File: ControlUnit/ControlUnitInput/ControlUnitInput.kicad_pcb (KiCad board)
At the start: 2 copper layers, 100.1 x 90 mm, 41 parts, among them J1 Conn_02x15_Odd_Even, J2 Conn_01x02, SW1 SW_Push, SW10 SW_Push, SW11 SW_Push, SW12 SW_Push, SW13 SW_Push, SW14 SW_Push, SW15 SW_Push, SW16 SW_Push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

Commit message: add schematic for LEDs controller
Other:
- board text added: "Board design by Keroth & CodingSpiderFox License: CERN OHL v1.2"
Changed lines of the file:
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@@
     (area 10.289181 12.624999 112.851001 102.775001)
     (thickness 1.6)
-    (drawings 4)
+    (drawings 5)
     (tracks 240)
     (zones 0)
@@
     )
   )
+  (gr_text "Board design by Keroth & CodingSpiderFox\nLicense: CERN OHL v1.2" (at 109.601 46.863 90) (layer F.Fab)
+    (effects (font (size 1.016 1.016) (thickness 0.254)))
+  )
   (gr_line (start 112.776 12.7) (end 112.776 102.7) (angle 90) (layer Edge.Cuts) (width 0.15))

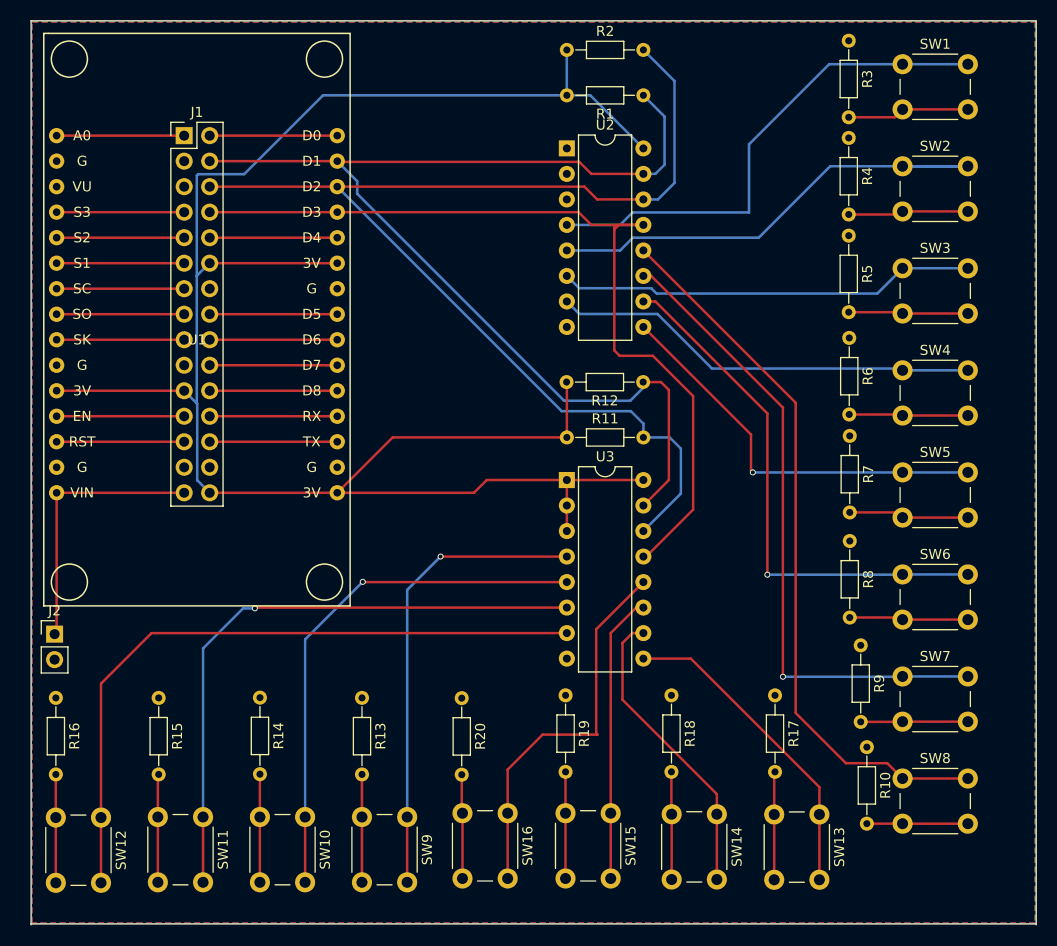
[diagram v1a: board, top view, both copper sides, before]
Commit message: clarify power connector voltages add license information and revisions to boards
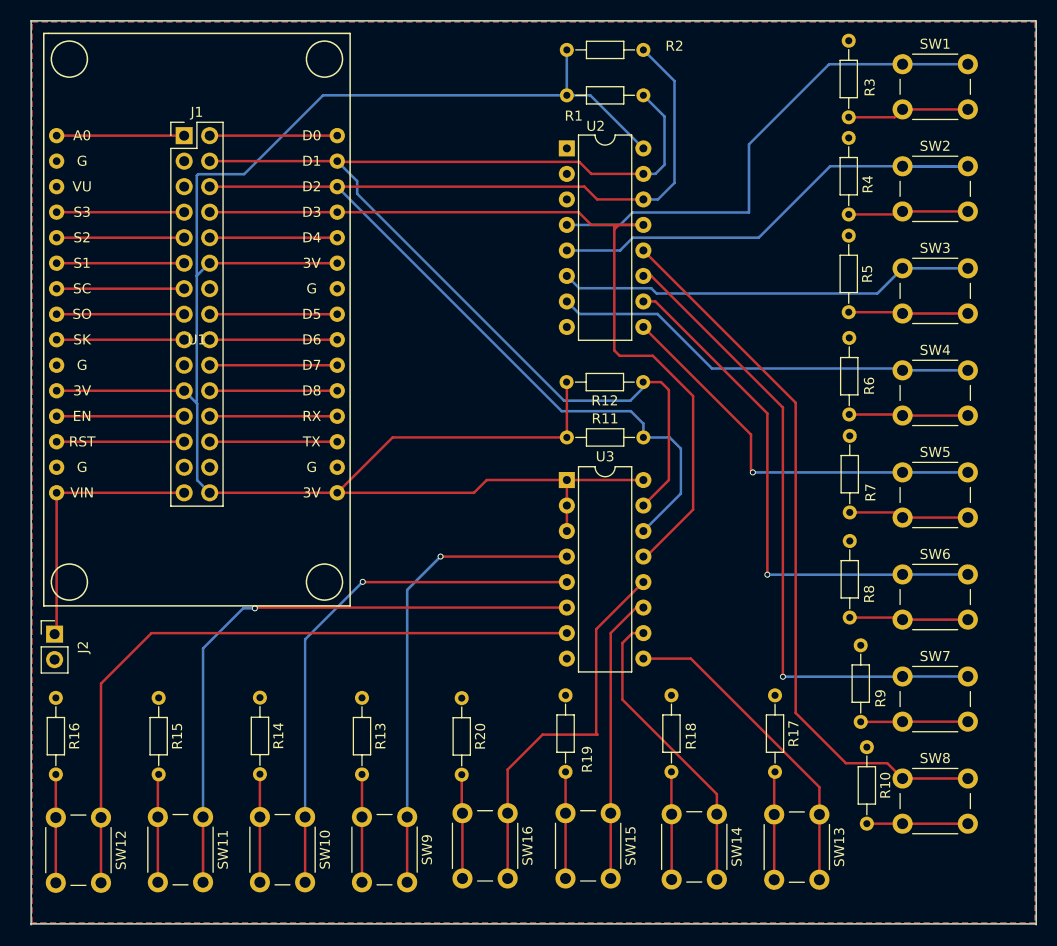
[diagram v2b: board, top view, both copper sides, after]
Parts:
- J1: value Conn_02x15_Odd_Even -> (none)
- J2: value Conn_01x02 -> (none)
- SW12: value SW_Push -> (none)
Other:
- board text added: "5V"
- board text added: "Rev 0.1"
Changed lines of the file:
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@@
     (links 139)
     (no_connects 0)
-    (area 10.289181 12.624999 112.851001 102.775001)
+    (area 11.9846 12.624999 112.851001 102.775001)
     (thickness 1.6)
-    (drawings 5)
+    (drawings 7)
     (tracks 240)
     (zones 0)
@@
       (effects (font (size 1 1) (thickness 0.15)))
     )
-    (fp_text value Conn_02x15_Odd_Even (at 1.27 37.89) (layer F.Fab)
+    (fp_text value "" (at 1.27 37.89) (layer F.Fab)
       (effects (font (size 1 1) (thickness 0.15)))
     )
@@
     (descr "Through hole straight pin header, 1x02, 2.54mm pitch, single row")
     (tags "Through hole pin header THT 1x02 2.54mm single row")
-    (fp_text reference J2 (at 0 -2.33) (layer F.SilkS)
-      (effects (font (size 1 1) (thickness 0.15)))
-    )
-    (fp_text value Conn_01x02 (at 0 4.87) (layer F.Fab)
+    (fp_text reference J2 (at 2.8448 1.2954 90) (layer F.SilkS)
+      (effects (font (size 1 1) (thickness 0.15)))
+    )
+    (fp_text value "" (at 0 4.87) (layer F.Fab)
       (effects (font (size 1 1) (thickness 0.15)))
     )
@@
     (descr "Resistor, Axial_DIN0204 series, Axial, Horizontal, pin pitch=7.62mm, 0.16666666666666666W = 1/6W, length*diameter=3.6*1.6mm^2, http://cdn-reichelt.de/documents/datenblatt/B400/1_4W%23YAG.pdf")
     (tags "Resistor Axial_DIN0204 series Axial Horizontal pin pitch 7.62mm 0.16666666666666666W = 1/6W length 3.6mm diameter 1.6mm")
-    (fp_text reference R1 (at 3.81 -1.86 180) (layer F.SilkS)
+    (fp_text reference R1 (at 6.9342 -2.0574 180) (layer F.SilkS)
       (effects (font (size 1 1) (thickness 0.15)))
     )
@@
     (descr "Resistor, Axial_DIN0204 series, Axial, Horizontal, pin pitch=7.62mm, 0.16666666666666666W = 1/6W, length*diameter=3.6*1.6mm^2, http://cdn-reichelt.de/documents/datenblatt/B400/1_4W%23YAG.pdf")
     (tags "Resistor Axial_DIN0204 series Axial Horizontal pin pitch 7.62mm 0.16666666666666666W = 1/6W length 3.6mm diameter 1.6mm")
-    (fp_text reference R2 (at 3.81 -1.86) (layer F.SilkS)
-      (effects (font (size 1 1) (thickness 0.15)))
-    )
-    (fp_text value 4.7k (at 3.81 1.86) (layer F.Fab)
+    (fp_text reference R2 (at 10.7188 -0.381) (layer F.SilkS)
+      (effects (font (size 1 1) (thickness 0.15)))
+    )
+    (fp_text value 4.7k (at -3.7846 -0.0254) (layer F.Fab)
       (effects (font (size 1 1) (thickness 0.15)))
     )
@@
     (descr "Resistor, Axial_DIN0204 series, Axial, Horizontal, pin pitch=7.62mm, 0.16666666666666666W = 1/6W, length*diameter=3.6*1.6mm^2, http://cdn-reichelt.de/documents/datenblatt/B400/1_4W%23YAG.pdf")
     (tags "Resistor Axial_DIN0204 series Axial Horizontal pin pitch 7.62mm 0.16666666666666666W = 1/6W length 3.6mm diameter 1.6mm")
-    (fp_text reference R3 (at 3.81 -1.86 270) (layer F.SilkS)
+    (fp_text reference R3 (at 4.6482 -2.1082 270) (layer F.SilkS)
       (effects (font (size 1 1) (thickness 0.15)))
     )
@@
     (descr "Resistor, Axial_DIN0204 series, Axial, Horizontal, pin pitch=7.62mm, 0.16666666666666666W = 1/6W, length*diameter=3.6*1.6mm^2, http://cdn-reichelt.de/documents/datenblatt/B400/1_4W%23YAG.pdf")
     (tags "Resistor Axial_DIN0204 series Axial Horizontal pin pitch 7.62mm 0.16666666666666666W = 1/6W length 3.6mm diameter 1.6mm")
-    (fp_text reference R4 (at 3.81 -1.86 270) (layer F.SilkS)
+    (fp_text reference R4 (at 4.6228 -1.905 270) (layer F.SilkS)
       (effects (font (size 1 1) (thickness 0.15)))
     )
@@
     (descr "Resistor, Axial_DIN0204 series, Axial, Horizontal, pin pitch=7.62mm, 0.16666666666666666W = 1/6W, length*diameter=3.6*1.6mm^2, http://cdn-reichelt.de/documents/datenblatt/B400/1_4W%23YAG.pdf")
     (tags "Resistor Axial_DIN0204 series Axial Horizontal pin pitch 7.62mm 0.16666666666666666W = 1/6W length 3.6mm diameter 1.6mm")
-    (fp_text reference R6 (at 3.81 -1.86 270) (layer F.SilkS)
+    (fp_text reference R6 (at 4.7752 -2.0066 270) (layer F.SilkS)
       (effects (font (size 1 1) (thickness 0.15)))
     )
@@
     (descr "Resistor, Axial_DIN0204 series, Axial, Horizontal, pin pitch=7.62mm, 0.16666666666666666W = 1/6W, length*diameter=3.6*1.6mm^2, http://cdn-reichelt.de/documents/datenblatt/B400/1_4W%23YAG.pdf")
     (tags "Resistor Axial_DIN0204 series Axial Horizontal pin pitch 7.62mm 0.16666666666666666W = 1/6W length 3.6mm diameter 1.6mm")
-    (fp_text reference R7 (at 3.81 -1.86 270) (layer F.SilkS)
+    (fp_text reference R7 (at 5.6388 -2.0828 270) (layer F.SilkS)
       (effects (font (size 1 1) (thickness 0.15)))
     )
@@
     (descr "Resistor, Axial_DIN0204 series, Axial, Horizontal, pin pitch=7.62mm, 0.16666666666666666W = 1/6W, length*diameter=3.6*1.6mm^2, http://cdn-reichelt.de/documents/datenblatt/B400/1_4W%23YAG.pdf")
     (tags "Resistor Axial_DIN0204 series Axial Horizontal pin pitch 7.62mm 0.16666666666666666W = 1/6W length 3.6mm diameter 1.6mm")
-    (fp_text reference R8 (at 3.81 -1.86 270) (layer F.SilkS)
+    (fp_text reference R8 (at 5.2832 -1.9558 270) (layer F.SilkS)
       (effects (font (size 1 1) (thickness 0.15)))
     )
@@
     (descr "Resistor, Axial_DIN0204 series, Axial, Horizontal, pin pitch=7.62mm, 0.16666666666666666W = 1/6W, length*diameter=3.6*1.6mm^2, http://cdn-reichelt.de/documents/datenblatt/B400/1_4W%23YAG.pdf")
     (tags "Resistor Axial_DIN0204 series Axial Horizontal pin pitch 7.62mm 0.16666666666666666W = 1/6W length 3.6mm diameter 1.6mm")
-    (fp_text reference R9 (at 3.81 -1.86 270) (layer F.SilkS)
+    (fp_text reference R9 (at 5.2832 -1.9812 270) (layer F.SilkS)
       (effects (font (size 1 1) (thickness 0.15)))
     )
@@
       (effects (font (size 1 1) (thickness 0.15)))
     )
-    (fp_text value 10k (at 3.81 1.86 270) (layer F.Fab)
+    (fp_text value 10k (at 0.4064 -2.1082 270) (layer F.Fab)
       (effects (font (size 1 1) (thickness 0.15)))
     )
@@
     (descr "Resistor, Axial_DIN0204 series, Axial, Horizontal, pin pitch=7.62mm, 0.16666666666666666W = 1/6W, length*diameter=3.6*1.6mm^2, http://cdn-reichelt.de/documents/datenblatt/B400/1_4W%23YAG.pdf")
     (tags "Resistor Axial_DIN0204 series Axial Horizontal pin pitch 7.62mm 0.16666666666666666W = 1/6W length 3.6mm diameter 1.6mm")
-    (fp_text reference R18 (at 3.81 -1.86 270) (layer F.SilkS)
+    (fp_text reference R18 (at 4.064 -1.9558 270) (layer F.SilkS)
       (effects (font (size 1 1) (thickness 0.15)))
     )
@@
     (descr "Resistor, Axial_DIN0204 series, Axial, Horizontal, pin pitch=7.62mm, 0.16666666666666666W = 1/6W, length*diameter=3.6*1.6mm^2, http://cdn-reichelt.de/documents/datenblatt/B400/1_4W%23YAG.pdf")
     (tags "Resistor Axial_DIN0204 series Axial Horizontal pin pitch 7.62mm 0.16666666666666666W = 1/6W length 3.6mm diameter 1.6mm")
-    (fp_text reference R19 (at 3.81 -1.86 270) (layer F.SilkS)
+    (fp_text reference R19 (at 6.3754 -2.159 270) (layer F.SilkS)
       (effects (font (size 1 1) (thickness 0.15)))
     )
@@
       (effects (font (size 1 1) (thickness 0.15)))
     )
-    (fp_text value SW_Push (at 3.75 6.7 270) (layer F.Fab)
+    (fp_text value "" (at 3.75 6.7 270) (layer F.Fab)
       (effects (font (size 1 1) (thickness 0.15)))
     )
@@
     (descr "16-lead though-hole mounted DIP package, row spacing 7.62 mm (300 mils)")
     (tags "THT DIP DIL PDIP 2.54mm 7.62mm 300mil")
-    (fp_text reference U2 (at 3.81 -2.33) (layer F.SilkS)
+    (fp_text reference U2 (at 2.8702 -2.2098) (layer F.SilkS)
       (effects (font (size 1 1) (thickness 0.15)))
     )
@@
     )
   )
+  (gr_text 5V (at 18.2372 72.898) (layer Eco2.User)
+    (effects (font (size 1.5 1.5) (thickness 0.3)))
+  )
+  (gr_text "Rev  0.1" (at 106.0704 99.8728) (layer Eco2.User)
+    (effects (font (size 1.5 1.5) (thickness 0.3)))
+  )
   (gr_text "Board design by Keroth & CodingSpiderFox\nLicense: CERN OHL v1.2" (at 109.601 46.863 90) (layer F.Fab)

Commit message: add additional connectors for NodeMCU pins in order to be able to connect additional input devices later on
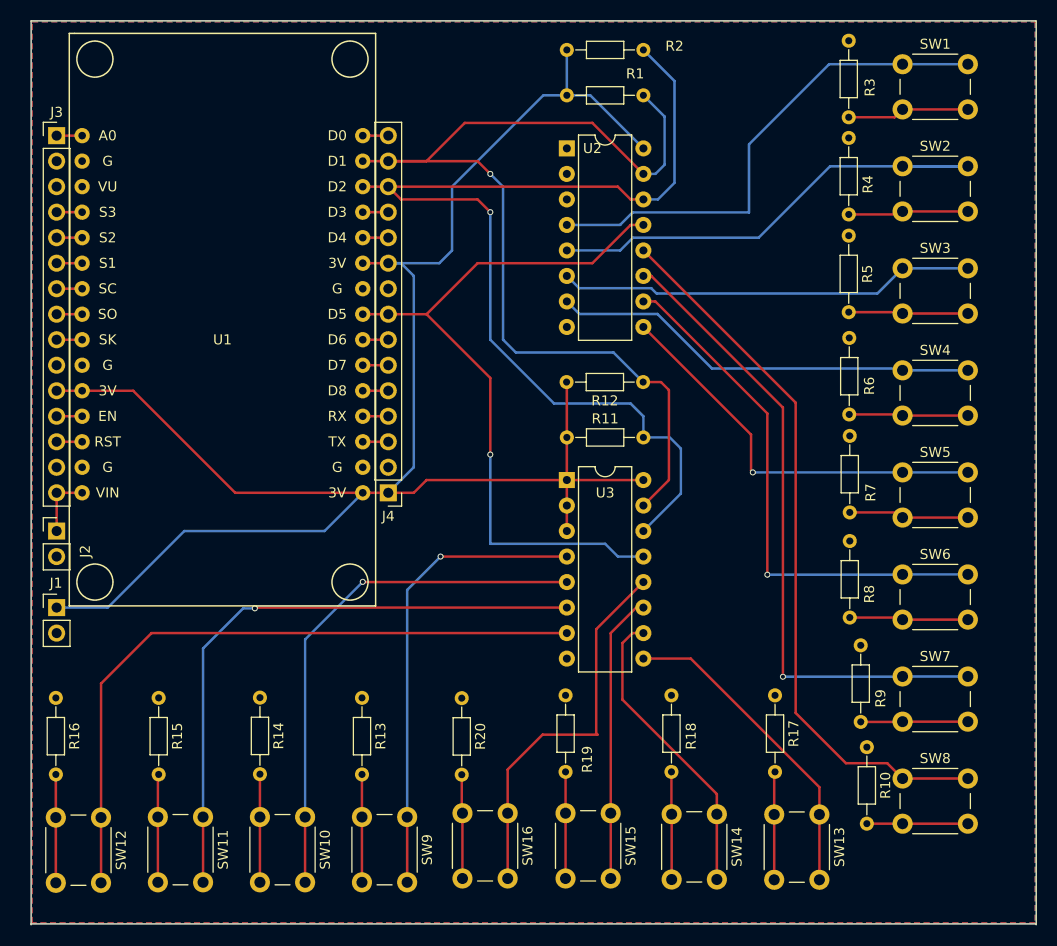
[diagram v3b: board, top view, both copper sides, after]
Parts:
- added J3: , Pin_Headers:Pin_Header_Straight_1x15_Pitch2.54mm, F.Cu at (15.2, 24.1)
- added J4: , Pin_Headers:Pin_Header_Straight_1x15_Pitch2.54mm, F.Cu at (48.3, 59.7)
- J1: footprint Pin_Headers:Pin_Header_Straight_2x15_Pitch2.54mm -> Pin_Headers:Pin_Header_Straight_1x02_Pitch2.54mm
- U2: value PCF8574 -> (none)
- moved J1 48.7 mm to (15.2, 71.1)
- moved J2 10.3 mm to (15.2, 63.5)
- moved U1 2.54 mm to (31.8, 44.5)
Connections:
- J1 pad 1: A0 -> +3V3
- J1 pad 2: D0 -> GND
- U1 pad 23: D5 -> INT
- U1 pad 27: INT -> D3
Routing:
- net +5V: track 26.9 -> 6.35 mm
- net INT: track 87.1 -> 73.2 mm, vias 0 -> 1
- net D5: track 12.7 -> 0.00 mm
- net SCL: track 117.6 -> 105.1 mm, vias 0 -> 1
- net +3V3: track 195.0 -> 184.2 mm
- net SDA: track 111.6 -> 101.4 mm, vias 0 -> 1
- net TX: track 12.7 -> 2.54 mm
- net SD3: track 12.7 -> 2.54 mm
- net SD2: track 12.7 -> 2.54 mm
- net RX: track 12.7 -> 2.54 mm
- net RST: track 12.7 -> 2.54 mm
- net MOSI: track 12.7 -> 2.54 mm
- net MISO: track 12.7 -> 2.54 mm
- net EN: track 12.7 -> 2.54 mm
- net D8: track 12.7 -> 2.54 mm
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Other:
- board text added: "3.3V"
- board text added: "Rev 0.2"
- board text removed: "Rev 0.1"

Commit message: realign components and fix track widths
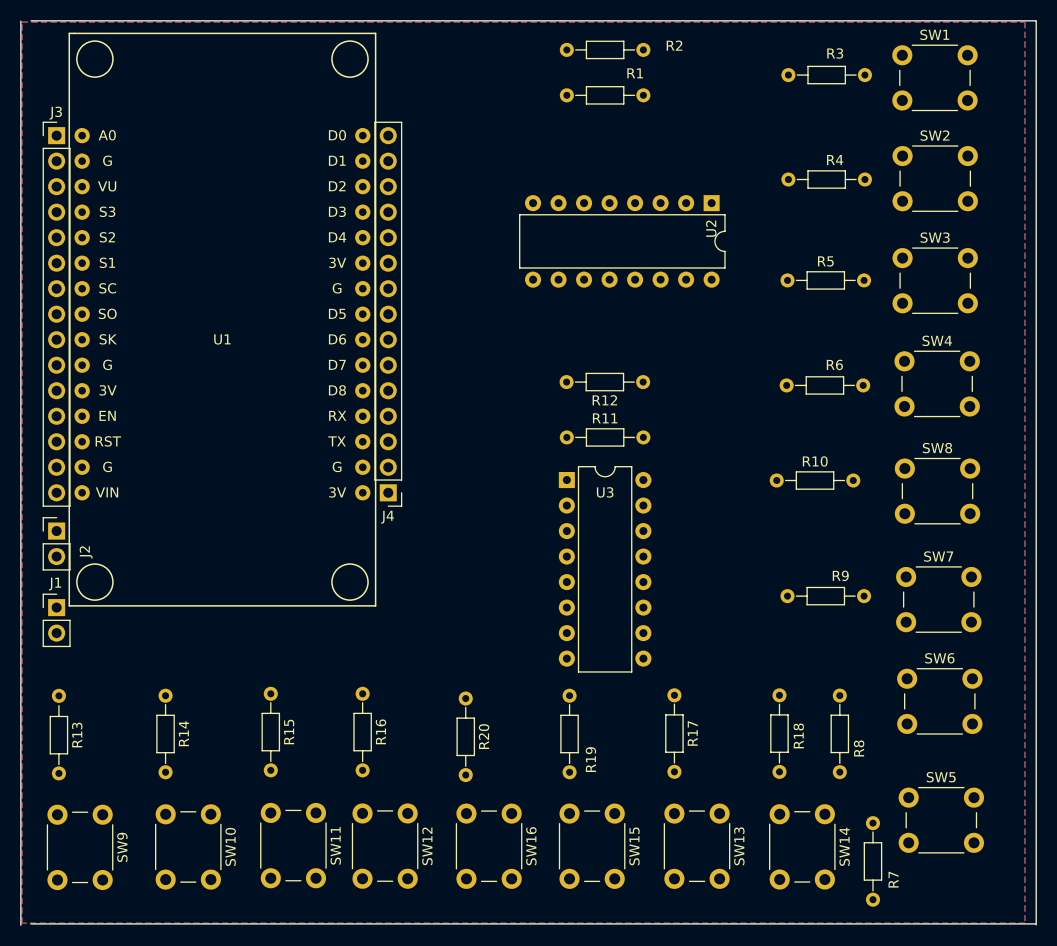
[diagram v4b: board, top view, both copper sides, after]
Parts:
- moved R7 38.6 mm to (96.5, 92.6)
- moved SW5 32.4 mm to (100.1, 90.0)
- moved SW8 30.9 mm to (99.7, 57.3)
- moved R16 30.5 mm to (45.7, 79.7)
- moved SW12 30.5 mm to (50.2, 91.6)
- moved SW9 30.3 mm to (19.8, 91.7)
- moved R13 30.2 mm to (15.5, 80.0)
- moved R10 28.0 mm to (86.9, 58.5), turned to 0 degrees
- moved R8 15.4 mm to (93.2, 79.9)
- moved U2 15.4 mm to (80.5, 30.8), turned to 270 degrees
- moved SW11 11.3 mm to (41.1, 91.6)
- moved R15 11.2 mm to (36.6, 79.7)
- moved R18 10.8 mm to (87.2, 79.9)
- moved SW14 10.8 mm to (91.7, 91.7)
- moved SW6 10.4 mm to (99.9, 78.2)
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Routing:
- net +3V3: track 184.2 -> 0.00 mm
- net SCL: track 105.1 -> 0.00 mm, vias 1 -> 0
- net SDA: track 101.4 -> 0.00 mm, vias 1 -> 0
- net INT: track 73.2 -> 0.00 mm, vias 1 -> 0
- net Net-(SW8-Pad1): track 72.2 -> 0.00 mm
- net Net-(SW12-Pad1): track 68.3 -> 0.00 mm
- net Net-(SW7-Pad1): track 64.5 -> 0.00 mm, vias 1 -> 0
- net Net-(SW11-Pad1): track 61.2 -> 0.00 mm, vias 1 -> 0
- net Net-(SW6-Pad1): track 53.0 -> 0.00 mm, vias 1 -> 0
- net Net-(SW10-Pad1): track 52.6 -> 0.00 mm, vias 1 -> 0
- net Net-(SW1-Pad1): track 50.5 -> 0.00 mm
- net Net-(SW2-Pad1): track 49.9 -> 0.00 mm
- net Net-(SW9-Pad1): track 46.4 -> 0.00 mm, vias 1 -> 0
- net Net-(SW4-Pad1): track 42.8 -> 0.00 mm
- net Net-(SW3-Pad1): track 41.7 -> 0.00 mm
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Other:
- board size 100.1 x 90 mm -> 101.1 x 90 mm
- net class Default: clearance 0.2 -> 0.3; trace_width 0.25 -> 0.5; via_dia 0.6 -> 0.8
- rule trace_clearance: 0.2 -> 0.3
- board text added: "Rev 0.3"
- board text removed: "Rev 0.2"
